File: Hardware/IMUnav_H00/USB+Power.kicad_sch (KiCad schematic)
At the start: 21 parts, among them U1 USB2514B-AEZC-TR, U4 TPS62823DLC, U5 USBLC6-2P6, U6 TVS0500DRV

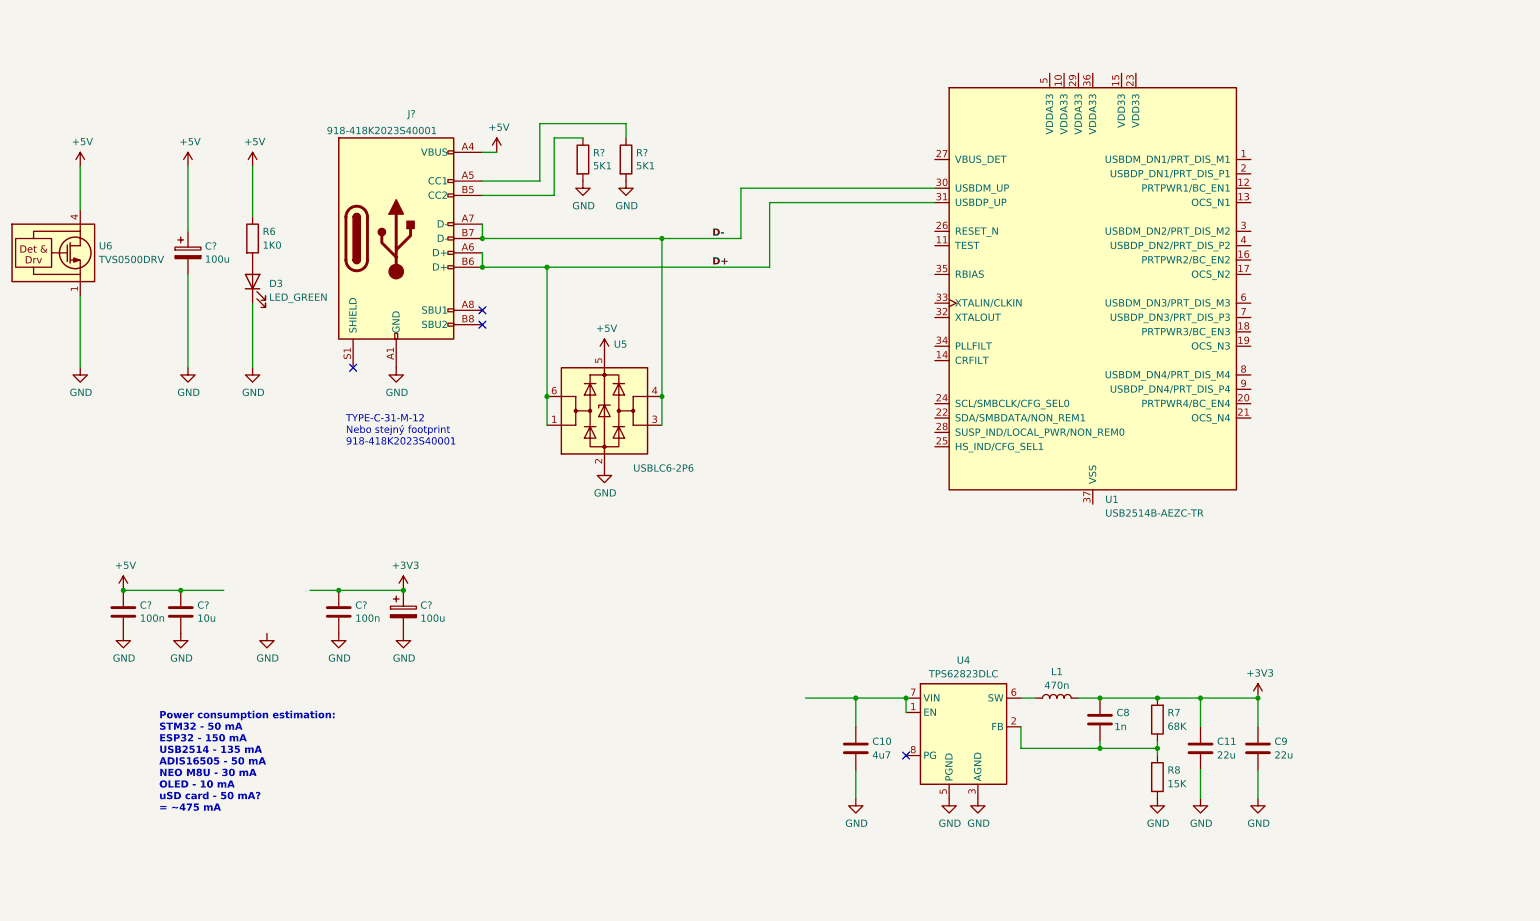
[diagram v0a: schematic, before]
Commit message: Finished USB Hub connection, added battery and power management. Added sheets for IMU and GPS.
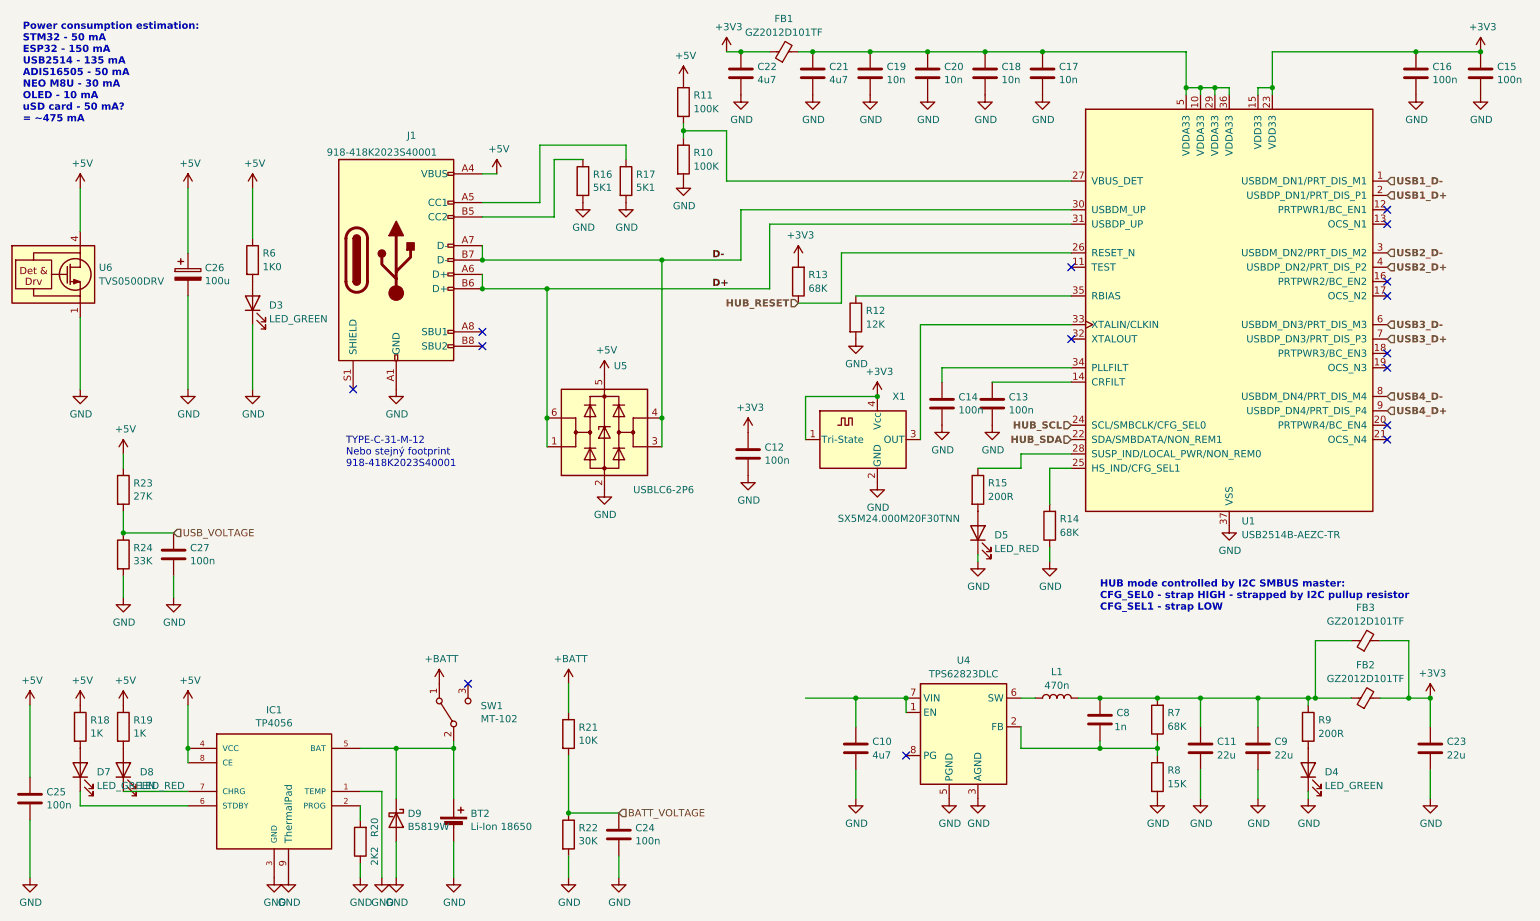
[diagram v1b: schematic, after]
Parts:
- removed C? (x2): 100n, Capacitor_SMD:C_0603_1608Metric, symbol Device:C
- removed C?: 10u, Capacitor_SMD:C_0805_2012Metric, symbol Device:C
- removed C?: 100u, Capacitor_THT:CP_Radial_D5.0mm_P2.00mm, symbol Device:C_Polarized
- added BT2: Li-Ion 18650, Battery:BatteryHolder_MPD_BH-18650-PC2, symbol Device:Battery_Cell
- added C12, C13, C14, C15, C16, C24, C25, C27: 100n, Capacitor_SMD:C_0603_1608Metric, symbol Device:C
- added C17, C18, C19, C20: 10n, Capacitor_SMD:C_0603_1608Metric, symbol Device:C
- added C21, C22: 4u7, Capacitor_SMD:C_0603_1608Metric, symbol Device:C
- added C23: 22u, Capacitor_SMD:C_0603_1608Metric, symbol Device:C
- added D4, D7: LED_GREEN, LED_SMD:LED_0603_1608Metric, symbol Device:LED
- added D5, D8: LED_RED, LED_SMD:LED_0603_1608Metric, symbol Device:LED
- added D9: B5819W, Diode_SMD:D_SOD-123, symbol Device:D_Schottky
- added FB1, FB2, FB3: GZ2012D101TF, Resistor_SMD:R_0805_2012Metric, symbol Device:FerriteBead_Small
- added IC1: TP4056, Package_SO:SOIC-8-1EP_3.9x4.9mm_P1.27mm_EP2.514x3.2mm_ThermalVias, symbol Sergej_Library:TP4056
- added R10, R11: 100K, Resistor_SMD:R_0603_1608Metric, symbol Device:R
- added R12: 12K, Resistor_SMD:R_0603_1608Metric, symbol Device:R
- added R13, R14: 68K, Resistor_SMD:R_0603_1608Metric, symbol Device:R
- added R15, R9: 200R, Resistor_SMD:R_0603_1608Metric, symbol Device:R
- added R18, R19: 1K, Resistor_SMD:R_0603_1608Metric, symbol Device:R
- added R20: 2K2, Resistor_SMD:R_0603_1608Metric, symbol Device:R
- added R21: 10K, Resistor_SMD:R_0603_1608Metric, symbol Device:R
- added R22: 30K, Resistor_SMD:R_0603_1608Metric, symbol Device:R
- added R23: 27K, Resistor_SMD:R_0603_1608Metric, symbol Device:R
- added R24: 33K, Resistor_SMD:R_0603_1608Metric, symbol Device:R
- added SW1: MT-102, IMUnav:TE_A101SYCQ04, symbol Switch:SW_SPDT
- added X1: SX5M24.000M20F30TNN, IMUnav:OSC_ECS-3963-250-BN-TR, symbol IMUnav:ECS-5032MV
- gave numbers to parts that had none: 4
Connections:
- net +3V3: now also U1.15 (VDD33), U1.23 (VDD33), C12.1, C15.1, C16.1, C22.1, C23.1, FB1.1, FB2.2, FB3.2, R13.2, X1.1 (Tri-State), X1.4 (Vcc); no longer C11.1, C8.1, C9.1, L1.2, R7.2
- net +5V: now also C25.1, IC1.4 (VCC), IC1.8 (CE), R11.1, R18.1, R19.1, R23.1
- net GND: now also U1.37 (VSS), BT2.2 (-), C12.2, C13.2, C14.2, C15.2, C16.2, C17.2, C18.2, C19.2, C20.2, C21.2, C22.2, C23.2, C24.2, C25.2, C27.2, D4.1 (K), D5.1 (K), D9.2 (A), IC1.1 (TEMP), IC1.3 (GND), IC1.9 (ThermalPad), R10.2, R12.2, R14.1, R20.1, R22.2, R24.2, X1.2 (GND)
- net USB1_D-: now reaches U1.1 (USBDM_DN1/PRT_DIS_M1)
- net at U1.10 (VDDA33): now also U1.29 (VDDA33), U1.36 (VDDA33), U1.5 (VDDA33), C17.1, C18.1, C19.1, C20.1, C21.1, FB1.2
- net at U1.14 (CRFILT): now also C13.1
- net USB1_D+: now reaches U1.2 (USBDP_DN1/PRT_DIS_P1)
- net HUB_SDA: now reaches U1.22 (SDA/SMBDATA/NON_REM1)
- net HUB_SCL: now reaches U1.24 (SCL/SMBCLK/CFG_SEL0)
- net at U1.25 (HS_IND/CFG_SEL1): now also R14.2
- net HUB_RESET: now reaches U1.26 (RESET_N)
- net HUB_RESET: now also R13.1
- net at U1.27 (VBUS_DET): now also R10.1, R11.2
- net at U1.28 (SUSP_IND/LOCAL_PWR/NON_REM0): now also R15.1
- net USB2_D-: now reaches U1.3 (USBDM_DN2/PRT_DIS_M2)
- net at U1.33 (XTALIN/CLKIN): now also X1.3 (OUT)
- net at U1.34 (PLLFILT): now also C14.1
- net at U1.35 (RBIAS): now also R12.1
- net USB2_D+: now reaches U1.4 (USBDP_DN2/PRT_DIS_P2)
- net USB3_D-: now reaches U1.6 (USBDM_DN3/PRT_DIS_M3)
- net USB3_D+: now reaches U1.7 (USBDP_DN3/PRT_DIS_P3)
- net USB4_D-: now reaches U1.8 (USBDM_DN4/PRT_DIS_M4)
- net USB4_D+: now reaches U1.9 (USBDP_DN4/PRT_DIS_P4)
- new net: C11.1, C8.1, C9.1, FB2.1, FB3.1, L1.2, R7.2, R9.1
- new net: D7.1 (K), IC1.6 (STDBY)
- new net: D7.2 (A), R18.2
- new net: D8.1 (K), IC1.7 (CHRG)
- new net: D8.2 (A), R19.2
- new net: BT2.1 (+), D9.1 (K), IC1.5 (BAT), SW1.2 (B)
- new net: IC1.2 (PROG), R20.2
- new net: D5.2 (A), R15.2
- new net: D4.2 (A), R9.2
- new net +BATT: R21.1, SW1.1 (A)
- new net BATT_VOLTAGE: C24.1, R21.2, R22.1
- new net USB_VOLTAGE: C27.1, R23.2, R24.1
- no-connect marks 4 -> 15
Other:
- note added: "HUB mode controlled by I2C SMBUS master: CFG_SEL0 - strap HIGH - strapped by I2C pullup resistor CFG_SEL1 - strap LOW"
- moved on the sheet: C26, D3, J1, R16, R17, R6, U1, U5, U6
